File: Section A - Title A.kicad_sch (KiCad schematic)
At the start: 0 parts

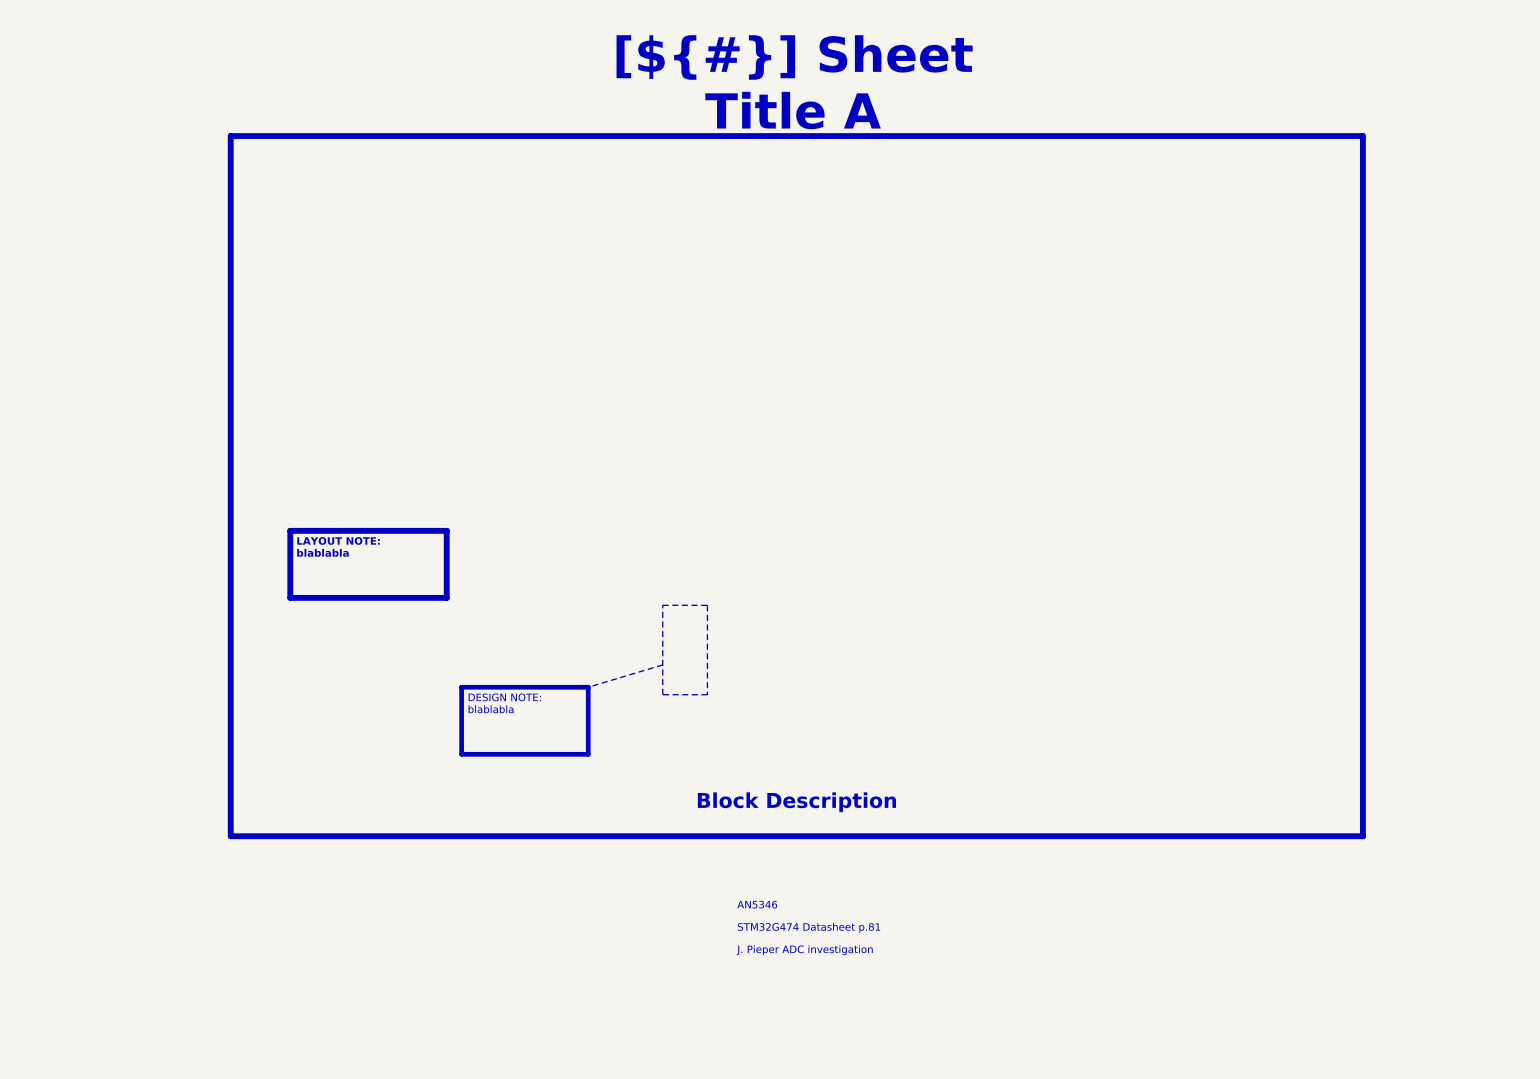
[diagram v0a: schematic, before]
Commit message: Initial commit: Moved over previous design and added isolation to CAN bus.
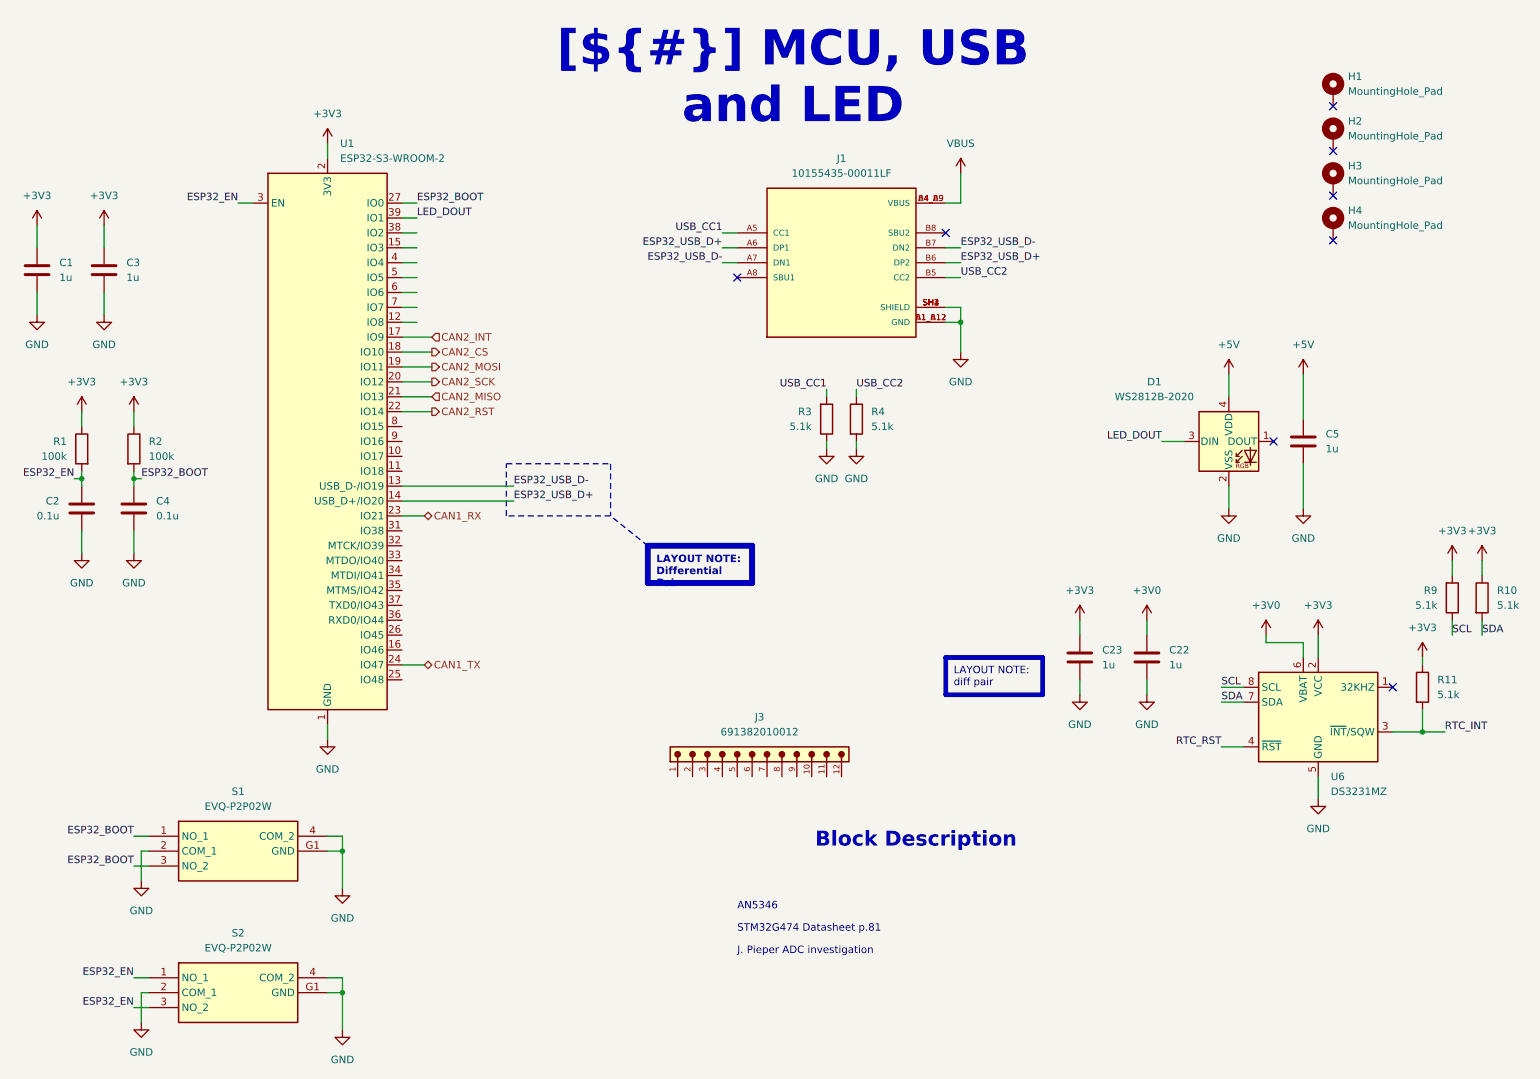
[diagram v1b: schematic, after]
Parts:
- added C1, C22, C23, C3, C5: 1u, Capacitor_SMD:C_0603_1608Metric_Pad1.08x0.95mm_HandSolder, symbol Device:C
- added C2, C4: 0.1u, Capacitor_SMD:C_0603_1608Metric_Pad1.08x0.95mm_HandSolder, symbol Device:C
- added D1: WS2812B-2020, LED_SMD:LED_WS2812B-2020_PLCC4_2.0x2.0mm, symbol LED:WS2812B-2020
- added H1, H2, H3, H4: MountingHole_Pad, MountingHole:MountingHole_3.2mm_M3_DIN965_Pad, symbol Mechanical:MountingHole_Pad
- added J1: 10155435-00011LF, 10155435-00011LF:AMPHENOL_10155435-00011LF, symbol 10155435-00011LF:10155435-00011LF
- added J3: 691382010012, 691382010012:691382010012, symbol 691382010012:691382010012
- added R1, R2: 100k, Resistor_SMD:R_0603_1608Metric_Pad0.98x0.95mm_HandSolder, symbol Device:R
- added R10, R11, R3, R4, R9: 5.1k, Resistor_SMD:R_0603_1608Metric_Pad0.98x0.95mm_HandSolder, symbol Device:R
- added S1, S2: EVQ-P2P02W, EVQ-P2P02W:EVQP2P02W, symbol EVQ-P2P02W:EVQ-P2P02W
- added U1: ESP32-S3-WROOM-2, RF_Module:ESP32-S3-WROOM-2, symbol RF_Module:ESP32-S3-WROOM-2
- added U6: DS3231MZ, Package_SO:SOIC-8_3.9x4.9mm_P1.27mm, symbol Timer_RTC:DS3231MZ
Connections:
- new net +3V0: C22.1, U6.6 (VBAT)
- new net +3V3: C1.1, C23.1, C3.1, R1.1, R10.1, R11.1, R2.1, R9.2, U1.2 (3V3), U6.2 (VCC)
- new net +5V: C5.1, D1.4 (VDD)
- new net CAN1_RX: U1.23 (IO21)
- new net CAN1_TX: U1.24 (IO47)
- new net CAN2_CS: U1.18 (IO10)
- new net CAN2_INT: U1.17 (IO9)
- new net CAN2_MISO: U1.21 (IO13)
- new net CAN2_MOSI: U1.19 (IO11)
- new net CAN2_RST: U1.22 (IO14)
- new net CAN2_SCK: U1.20 (IO12)
- new net ESP32_BOOT: C4.1, R2.2, S1.1 (NO_1), S1.3 (NO_2), U1.27 (IO0)
- new net ESP32_EN: C2.1, R1.2, S2.1 (NO_1), S2.3 (NO_2), U1.3 (EN)
- new net ESP32_USB_D+: J1.A6 (DP1), J1.B6 (DP2), U1.14 (USB_D+/IO20)
- new net ESP32_USB_D-: J1.A7 (DN1), J1.B7 (DN2), U1.13 (USB_D-/IO19)
- new net GND: C1.2, C2.2, C22.2, C23.2, C3.2, C4.2, C5.2, D1.2 (VSS), J1.A1_B12 (GND), J1.B1_A12 (GND), J1.SH1 (SHIELD), J1.SH2 (SHIELD), J1.SH3 (SHIELD), J1.SH4 (SHIELD), R3.1, R4.2, S1.2 (COM_1), S1.4 (COM_2), S1.G1 (GND), S2.2 (COM_1), S2.4 (COM_2), S2.G1 (GND), U1.1 (GND), U1.40 (GND), U1.41 (GND), U6.5 (GND)
- new net LED_DOUT: D1.3 (DIN), U1.39 (IO1)
- new net RTC_INT: R11.2, U6.3 (~{INT}/SQW)
- new net RTC_RST: U6.4 (~{RST})
- new net SCL: R9.1, U6.8 (SCL)
- new net SDA: R10.2, U6.7 (SDA)
- new net USB_CC1: J1.A5 (CC1), R3.2
- new net USB_CC2: J1.B5 (CC2), R4.1
- new net VBUS: J1.A4_B9 (VBUS), J1.B4_A9 (VBUS)
- no-connect marks 0 -> 8
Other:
- title: Sheet Title A -> MCU, USB and LED
